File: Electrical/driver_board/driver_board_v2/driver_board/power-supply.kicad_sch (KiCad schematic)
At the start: 1 part, among them J2 Screw_Terminal_01x02

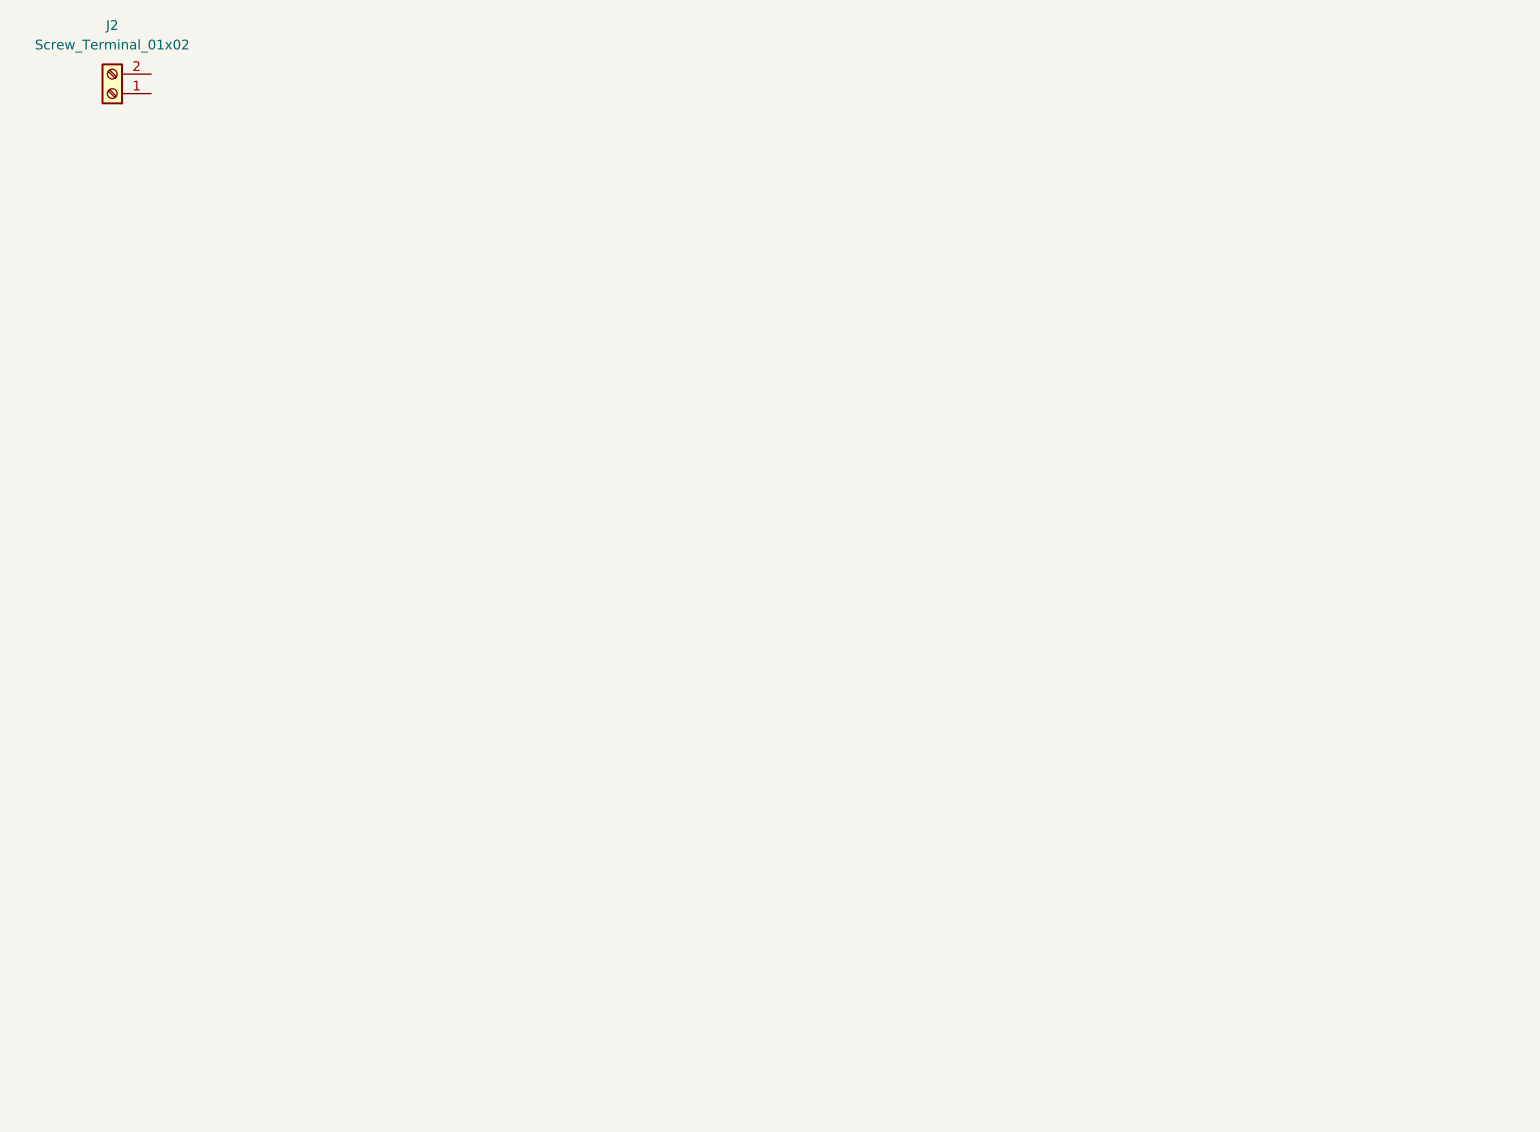
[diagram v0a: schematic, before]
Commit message: Added full PSU architecture to driverboard
+24V In

+12V out
+5V out
+3.3V out
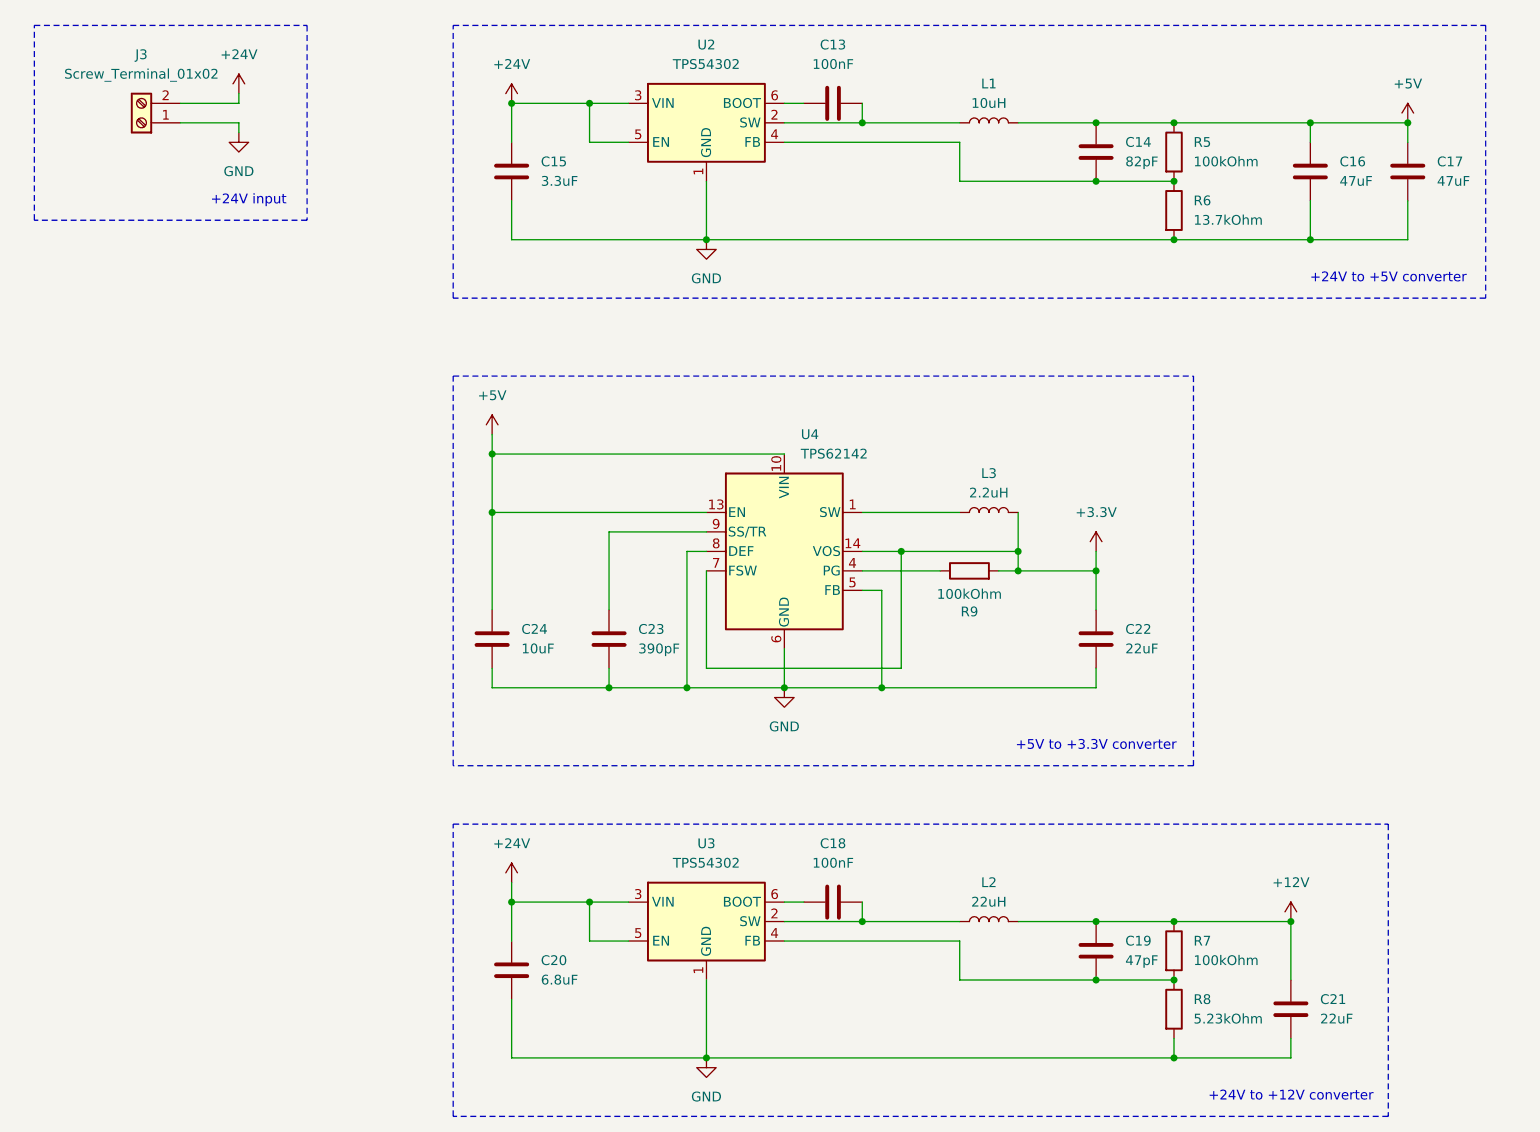
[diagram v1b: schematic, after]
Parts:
- added C13, C18: 100nF, symbol Device:C
- added C14: 82pF, symbol Device:C
- added C15: 3.3uF, symbol Device:C
- added C16, C17: 47uF, symbol Device:C
- added C19: 47pF, symbol Device:C
- added C20: 6.8uF, symbol Device:C
- added C21, C22: 22uF, symbol Device:C
- added C23: 390pF, symbol Device:C
- added C24: 10uF, symbol Device:C
- added L1: 10uH, symbol Device:L
- added L2: 22uH, symbol Device:L
- added L3: 2.2uH, symbol Device:L
- added R5, R7, R9: 100kOhm, symbol Device:R
- added R6: 13.7kOhm, symbol Device:R
- added R8: 5.23kOhm, symbol Device:R
- added U2, U3: TPS54302, Package_TO_SOT_SMD:SOT-23-6, symbol Regulator_Switching:TPS54302
- added U4: TPS62142, Package_DFN_QFN:VQFN-16-1EP_3x3mm_P0.5mm_EP1.68x1.68mm_ThermalVias, symbol Regulator_Switching:TPS62142
- renumbered J2 to J3
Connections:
- net GND: now reaches J3.1 (Pin_1)
- net GND: now also C15.2, C16.2, C17.2, C20.2, C21.2, C22.1, C23.1, C24.1, R6.2, R8.2, U2.1 (GND), U3.1 (GND), U4.15 (GND), U4.16 (GND), U4.17 (GND), U4.5 (FB), U4.6 (GND), U4.8 (DEF)
- net +24V: now reaches J3.2 (Pin_2)
- net +24V: now also C15.1, C20.1, U2.3 (VIN), U2.5 (EN), U3.3 (VIN), U3.5 (EN)
- new net: C14.1, R5.2, R6.1, U2.4 (FB)
- new net: C18.2, L2.1, U3.2 (SW)
- new net: C19.1, R7.2, R8.1, U3.4 (FB)
- new net: C18.1, U3.6 (BOOT)
- new net: C13.2, L1.1, U2.2 (SW)
- new net: C13.1, U2.6 (BOOT)
- new net: R9.1, U4.4 (PG)
- new net: C23.2, U4.9 (SS/TR)
- new net: L3.1, U4.1 (SW), U4.2 (SW), U4.3 (SW)
- new net +12V: C19.2, C21.1, L2.2, R7.1
- new net +3.3V: C22.2, L3.2, R9.2, U4.14 (VOS), U4.7 (FSW)
- new net +5V: C14.2, C16.1, C17.1, C24.2, L1.2, R5.1, U4.10 (VIN), U4.11 (VIN), U4.12 (VIN), U4.13 (EN)
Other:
- note added: "+24V input"
- note added: "+24V to +12V converter"
- note added: "+24V to +5V converter"
- note added: "+5V to +3.3V converter"
- moved on the sheet: J3

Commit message: Added footprint of motor driver and added power
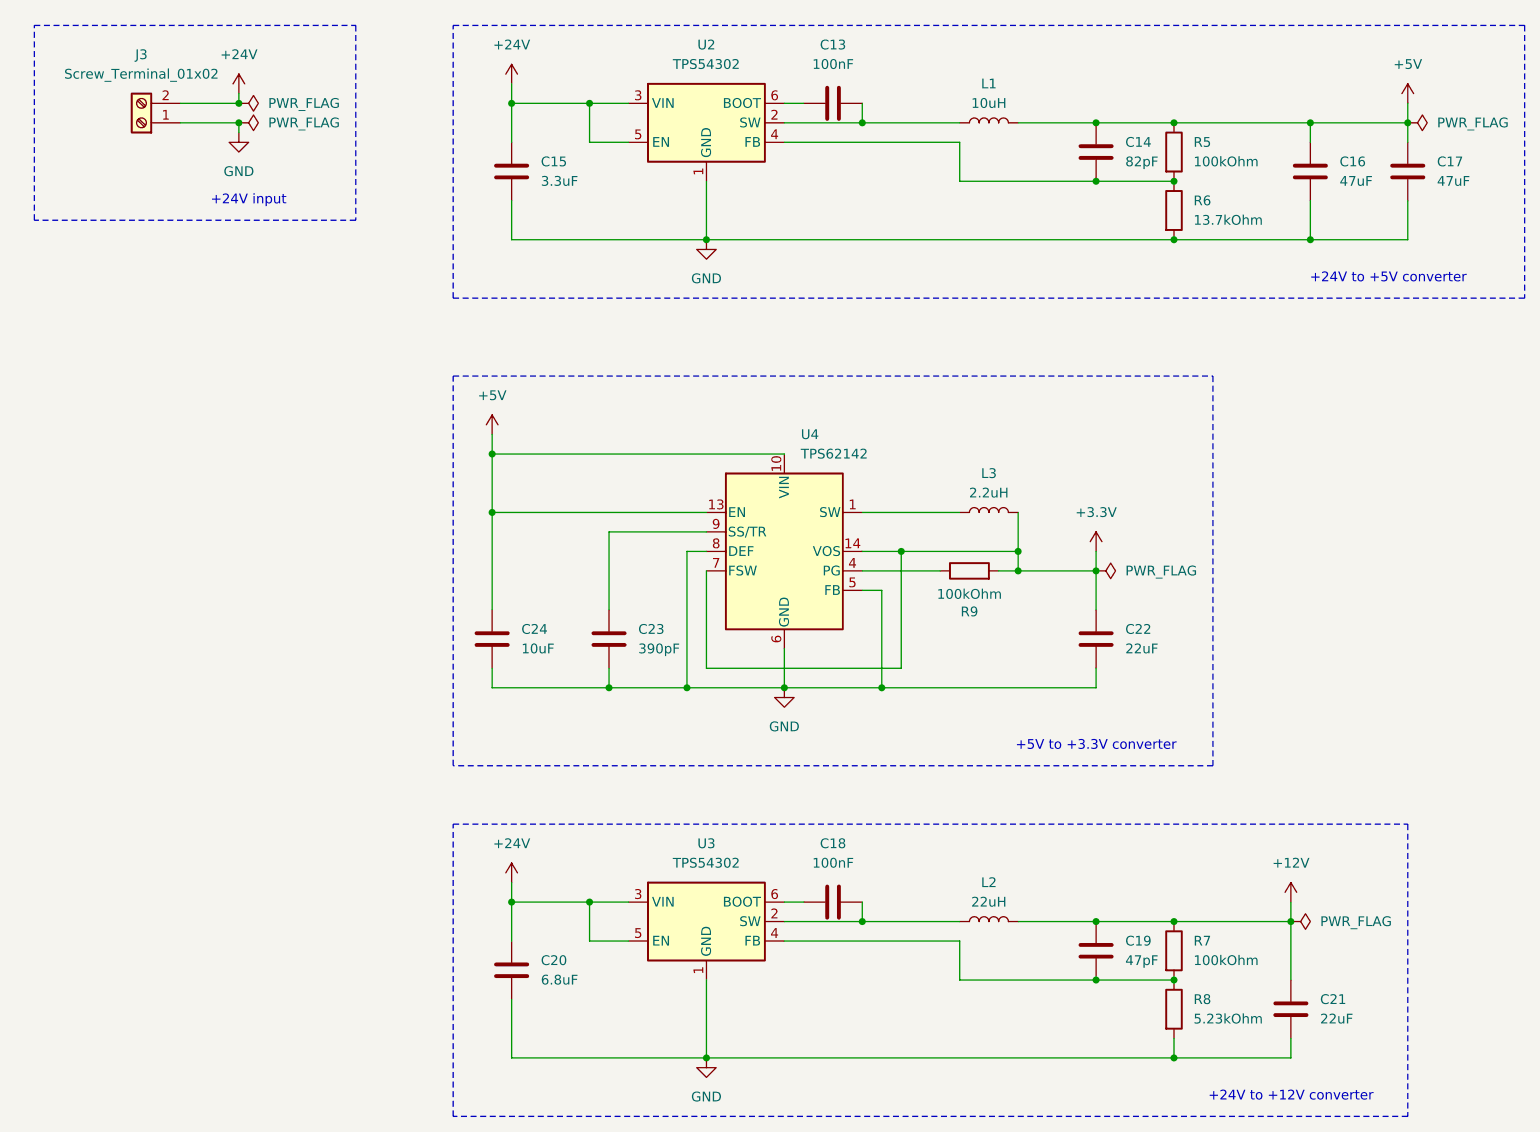
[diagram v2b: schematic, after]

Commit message: restructure
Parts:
- renumbered C24 to C1, C21 to C10, C16 to C11, C17 to C12, C15 to C2, C20 to C3, C23 to C4, C13 to C5, C18 to C6, C14 to C7, C22 to C8, C19 to C9, J3 to J1, L3 to L2, L2 to L3, R9 to R1, R5 to R2, R6 to R3, R7 to R4, R8 to R5, U2 to U1, U3 to U2, U4 to U3

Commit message: Discovered critical error and changed pinout
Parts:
- renumbered C5 to C13, C7 to C14, C2 to C15, C11 to C16, C12 to C17, C6 to C18, C9 to C19, C3 to C20, C10 to C21, C8 to C22, C4 to C23, C1 to C24, J1 to J3, L3 to L2, L2 to L3, R2 to R5, R3 to R6, R4 to R7, R5 to R8, R1 to R9, U1 to U2, U2 to U3, U3 to U4
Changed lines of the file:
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@@
 		(dnp no)
 		(fields_autoplaced yes)
-		(property "Reference" "C12"
+		(property "Reference" "C17"
 			(at 199.39 35.5599 0)
 			(effects
@@
 		(dnp no)
 		(fields_autoplaced yes)
-		(property "Reference" "#PWR0109"
+		(property "Reference" "#PWR017"
 			(at 195.58 31.75 0)
 			(effects
@@
 		(dnp no)
 		(fields_autoplaced yes)
-		(property "Reference" "R3"
+		(property "Reference" "R6"
 			(at 167.64 40.6399 0)
 			(effects
@@
 		(dnp no)
 		(fields_autoplaced yes)
-		(property "Reference" "U2"
+		(property "Reference" "U3"
 			(at 104.14 124.46 0)
 			(effects
@@
 		(dnp no)
 		(fields_autoplaced yes)
-		(property "Reference" "C8"
+		(property "Reference" "C22"
 			(at 158.75 96.5199 0)
 			(effects
@@
 		(dnp no)
 		(fields_autoplaced yes)
-		(property "Reference" "C1"
+		(property "Reference" "C24"
 			(at 80.01 96.5199 0)
 			(effects
@@
 		(dnp no)
 		(fields_autoplaced yes)
-		(property "Reference" "J1"
+		(property "Reference" "J3"
 			(at 30.48 21.59 0)
 			(effects
@@
 		(dnp no)
 		(fields_autoplaced yes)
-		(property "Reference" "#PWR0105"
+		(property "Reference" "#PWR027"
 			(at 154.94 90.17 0)
 			(effects
@@
 		(dnp no)
 		(fields_autoplaced yes)
-		(property "Reference" "#PWR0103"
+		(property "Reference" "#PWR020"
 			(at 104.14 158.75 0)
 			(effects
@@
 		(dnp no)
 		(fields_autoplaced yes)
-		(property "Reference" "#PWR0104"
+		(property "Reference" "#PWR019"
 			(at 180.34 135.89 0)
 			(effects
@@
 		(dnp no)
 		(fields_autoplaced yes)
-		(property "Reference" "C6"
+		(property "Reference" "C18"
 			(at 120.65 124.46 90)
 			(effects
@@
 		(dnp no)
 		(fields_autoplaced yes)
-		(property "Reference" "#FLG0104"
+		(property "Reference" "#FLG03"
 			(at 156.845 88.9 0)
 			(effects
@@
 		(dnp no)
 		(fields_autoplaced yes)
-		(property "Reference" "U1"
+		(property "Reference" "U2"
 			(at 104.14 20.32 0)
 			(effects
@@
 		(dnp no)
 		(fields_autoplaced yes)
-		(property "Reference" "L3"
+		(property "Reference" "L2"
 			(at 140.97 129.54 90)
 			(effects
@@
 		(on_board yes)
 		(dnp no)
-		(property "Reference" "R1"
+		(property "Reference" "R9"
 			(at 138.43 94.234 90)
 			(effects
@@
 		(dnp no)
 		(fields_autoplaced yes)
-		(property "Reference" "R4"
+		(property "Reference" "R7"
 			(at 167.64 137.1599 0)
 			(effects
@@
 		(dnp no)
 		(fields_autoplaced yes)
-		(property "Reference" "C3"
+		(property "Reference" "C20"
 			(at 82.55 139.6999 0)
 			(effects
@@
 		(dnp no)
 		(fields_autoplaced yes)
-		(property "Reference" "#FLG0103"
+		(property "Reference" "#FLG02"
 			(at 182.245 134.62 0)
 			(effects
@@
 		(dnp no)
 		(fields_autoplaced yes)
-		(property "Reference" "C2"
+		(property "Reference" "C15"
 			(at 82.55 35.5599 0)
 			(effects
@@
 		(dnp no)
 		(fields_autoplaced yes)
-		(property "Reference" "#PWR0101"
+		(property "Reference" "#PWR021"
 			(at 43.18 30.48 0)
 			(effects
@@
 		(dnp no)
 		(fields_autoplaced yes)
-		(property "Reference" "#PWR0111"
+		(property "Reference" "#PWR018"
 			(at 104.14 52.07 0)
 			(effects
@@
 		(dnp no)
 		(fields_autoplaced yes)
-		(property "Reference" "C11"
+		(property "Reference" "C16"
 			(at 186.69 35.5599 0)
 			(effects
@@
 		(dnp no)
 		(fields_autoplaced yes)
-		(property "Reference" "#PWR0108"
+		(property "Reference" "#PWR025"
 			(at 114.3 110.49 0)
 			(effects
@@
 		(dnp no)
 		(fields_autoplaced yes)
-		(property "Reference" "C4"
+		(property "Reference" "C23"
 			(at 95.25 96.5199 0)
 			(effects
@@
 		(dnp no)
 		(fields_autoplaced yes)
-		(property "Reference" "U3"
+		(property "Reference" "U4"
 			(at 116.4433 71.12 0)
 			(effects
@@
 		(dnp no)
 		(fields_autoplaced yes)
-		(property "Reference" "#PWR0106"
+		(property "Reference" "#PWR026"
 			(at 76.2 74.93 0)
 			(effects
@@
 		(dnp no)
 		(fields_autoplaced yes)
-		(property "Reference" "#PWR0102"
+		(property "Reference" "#PWR022"
 			(at 43.18 38.1 0)
 			(effects
@@
 		(dnp no)
 		(fields_autoplaced yes)
-		(property "Reference" "C10"
+		(property "Reference" "C21"
 			(at 184.15 144.7799 0)
 			(effects
@@
 		(dnp no)
 		(fields_autoplaced yes)
-		(property "Reference" "#PWR0110"
+		(property "Reference" "#PWR023"
 			(at 78.74 29.21 0)
 			(effects
@@
 		(dnp no)
 		(fields_autoplaced yes)
-		(property "Reference" "L2"
+		(property "Reference" "L3"
 			(at 140.97 76.2 90)
 			(effects
@@
 		(dnp no)
 		(fields_autoplaced yes)
-		(property "Reference" "C7"
+		(property "Reference" "C14"
 			(at 158.75 33.0199 0)
 			(effects
@@
 		(dnp no)
 		(fields_autoplaced yes)
-		(property "Reference" "R5"
+		(property "Reference" "R8"
 			(at 167.64 144.7799 0)
 			(effects
@@
 		(dnp no)
 		(fields_autoplaced yes)
-		(property "Reference" "C9"
+		(property "Reference" "C19"
 			(at 158.75 137.1599 0)
 			(effects
@@
 		(dnp no)
 		(fields_autoplaced yes)
-		(property "Reference" "C5"
+		(property "Reference" "C13"
 			(at 120.65 20.32 90)
 			(effects
@@
 		(dnp no)
 		(fields_autoplaced yes)
-		(property "Reference" "#FLG0101"
+		(property "Reference" "#FLG01"
 			(at 45.085 27.94 0)
 			(effects
@@
 		(dnp no)
 		(fields_autoplaced yes)
-		(property "Reference" "#FLG0102"
+		(property "Reference" "#FLG05"
 			(at 45.085 30.48 0)
 			(effects
@@
 		(dnp no)
 		(fields_autoplaced yes)
-		(property "Reference" "#FLG0105"
+		(property "Reference" "#FLG06"
 			(at 197.485 30.48 0)
 			(effects
@@
 		(dnp no)
 		(fields_autoplaced yes)
-		(property "Reference" "#PWR0107"
+		(property "Reference" "#PWR024"
 			(at 78.74 133.35 0)
 			(effects
@@
 		(dnp no)
 		(fields_autoplaced yes)
-		(property "Reference" "R2"
+		(property "Reference" "R5"
 			(at 167.64 33.0199 0)
 			(effects

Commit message: Added gripper
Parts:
- renumbered C24 to C18, C23 to C19, C22 to C20, C18 to C21, C19 to C22, C20 to C23, C21 to C24, L3 to L2, L2 to L3, R8 to R10, R5 to R6, R6 to R7, R9 to R8, R7 to R9, U4 to U3, U3 to U4
